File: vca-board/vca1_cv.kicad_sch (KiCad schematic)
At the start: 9 parts, among them U3 TL074

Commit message: VCA components linked
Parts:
- C10: footprint (none) -> Capacitor_SMD:C_0603_1608Metric_Pad1.08x0.95mm_HandSolder; LCSC (none) -> C76711
- C9: footprint (none) -> Capacitor_SMD:C_0603_1608Metric_Pad1.08x0.95mm_HandSolder; LCSC (none) -> C91367
- D3: footprint (none) -> Diode_SMD:D_SOD-523; LCSC (none) -> C131797
- D4: footprint (none) -> Diode_SMD:D_SOD-123; LCSC (none) -> C81598
- R21: footprint (none) -> Resistor_SMD:R_0201_0603Metric_Pad0.64x0.40mm_HandSolder; LCSC (none) -> C25811
- R24: footprint (none) -> Resistor_SMD:R_0201_0603Metric_Pad0.64x0.40mm_HandSolder; LCSC (none) -> C25803
- R25: LCSC (none) -> C22775
- R26: LCSC (none) -> C25804
- U3: footprint (none) -> Package_SO:SOIC-14_3.9x8.7mm_P1.27mm; LCSC (none) -> C6963
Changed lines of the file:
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@@
     (property "Reference" "R24" (id 0) (at 83.82 31.75 90))
     (property "Value" "100k" (id 1) (at 83.82 34.29 90))
-    (property "Footprint" "" (id 2) (at 83.82 39.878 90)
+    (property "Footprint" "Resistor_SMD:R_0201_0603Metric_Pad0.64x0.40mm_HandSolder" (id 2) (at 83.82 39.878 90)
       (effects (font (size 1.27 1.27)) hide)
     )
     (property "Datasheet" "~" (id 3) (at 83.82 38.1 0)
+      (effects (font (size 1.27 1.27)) hide)
+    )
+    (property "LCSC" "C25803" (id 4) (at 83.82 38.1 0)
       (effects (font (size 1.27 1.27)) hide)
     )
@@
       (effects (font (size 1.27 1.27)) hide)
     )
+    (property "LCSC" "C22775" (id 4) (at 99.06 53.34 0)
+      (effects (font (size 1.27 1.27)) hide)
+    )
     (pin "1")
     (pin "2")
@@
       (effects (font (size 1.27 1.27)) (justify left))
     )
-    (property "Footprint" "" (id 2) (at 106.68 66.04 0)
+    (property "Footprint" "Diode_SMD:D_SOD-523" (id 2) (at 106.68 66.04 0)
       (effects (font (size 1.27 1.27)) hide)
     )
     (property "Datasheet" "~" (id 3) (at 106.68 66.04 0)
+      (effects (font (size 1.27 1.27)) hide)
+    )
+    (property "LCSC" "C131797" (id 4) (at 106.68 66.04 0)
       (effects (font (size 1.27 1.27)) hide)
     )
@@
     (property "Reference" "C9" (id 0) (at 83.82 17.78 90))
     (property "Value" "10p" (id 1) (at 83.82 20.32 90))
-    (property "Footprint" "" (id 2) (at 87.63 24.4348 0)
+    (property "Footprint" "Capacitor_SMD:C_0603_1608Metric_Pad1.08x0.95mm_HandSolder" (id 2) (at 87.63 24.4348 0)
       (effects (font (size 1.27 1.27)) hide)
     )
@@
       (effects (font (size 1.27 1.27)) hide)
     )
+    (property "LCSC" "C91367" (id 4) (at 83.82 25.4 0)
+      (effects (font (size 1.27 1.27)) hide)
+    )
     (pin "1")
     (pin "2")
@@
     )
     (property "Datasheet" "~" (id 3) (at 140.97 60.96 0)
+      (effects (font (size 1.27 1.27)) hide)
+    )
+    (property "LCSC" "C25804" (id 4) (at 140.97 60.96 0)
       (effects (font (size 1.27 1.27)) hide)
     )
@@
     (property "Reference" "U3" (id 0) (at 119.38 40.64 0))
     (property "Value" "TL074" (id 1) (at 119.38 43.18 0))
-    (property "Footprint" "" (id 2) (at 118.11 53.34 0)
+    (property "Footprint" "Package_SO:SOIC-14_3.9x8.7mm_P1.27mm" (id 2) (at 118.11 53.34 0)
       (effects (font (size 1.27 1.27)) hide)
     )
     (property "Datasheet" "http://www.ti.com/lit/ds/symlink/tl071.pdf" (id 3) (at 120.65 55.88 0)
+      (effects (font (size 1.27 1.27)) hide)
+    )
+    (property "LCSC" "C6963" (id 4) (at 119.38 50.8 0)
       (effects (font (size 1.27 1.27)) hide)
     )
@@
       (effects (font (size 1.27 1.27)) (justify right))
     )
-    (property "Footprint" "" (id 2) (at 204.7748 46.99 0)
+    (property "Footprint" "Capacitor_SMD:C_0603_1608Metric_Pad1.08x0.95mm_HandSolder" (id 2) (at 204.7748 46.99 0)
       (effects (font (size 1.27 1.27)) hide)
     )
     (property "Datasheet" "~" (id 3) (at 205.74 50.8 0)
+      (effects (font (size 1.27 1.27)) hide)
+    )
+    (property "LCSC" "C76711" (id 4) (at 205.74 50.8 0)
       (effects (font (size 1.27 1.27)) hide)
     )
@@
     (property "Reference" "R21" (id 0) (at 68.58 44.45 90))
     (property "Value" "200k" (id 1) (at 68.58 46.99 90))
-    (property "Footprint" "" (id 2) (at 68.58 52.578 90)
+    (property "Footprint" "Resistor_SMD:R_0201_0603Metric_Pad0.64x0.40mm_HandSolder" (id 2) (at 68.58 52.578 90)
       (effects (font (size 1.27 1.27)) hide)
     )
@@
       (effects (font (size 1.27 1.27)) hide)
     )
+    (property "LCSC" "C25811" (id 4) (at 68.58 50.8 0)
+      (effects (font (size 1.27 1.27)) hide)
+    )
     (pin "1")
     (pin "2")
@@
       (effects (font (size 1.27 1.27)) (justify left))
     )
-    (property "Footprint" "" (id 2) (at 217.17 48.26 0)
+    (property "Footprint" "Package_SO:SOIC-14_3.9x8.7mm_P1.27mm" (id 2) (at 217.17 48.26 0)
       (effects (font (size 1.27 1.27)) hide)
     )
     (property "Datasheet" "http://www.ti.com/lit/ds/symlink/tl071.pdf" (id 3) (at 219.71 45.72 0)
+      (effects (font (size 1.27 1.27)) hide)
+    )
+    (property "LCSC" "C6963" (id 4) (at 218.44 50.8 0)
       (effects (font (size 1.27 1.27)) hide)
     )
@@
     (property "Reference" "D4" (id 0) (at 134.62 44.45 0))
     (property "Value" "D" (id 1) (at 134.62 46.99 0))
-    (property "Footprint" "" (id 2) (at 134.62 50.8 0)
+    (property "Footprint" "Diode_SMD:D_SOD-123" (id 2) (at 134.62 50.8 0)
       (effects (font (size 1.27 1.27)) hide)
     )
     (property "Datasheet" "~" (id 3) (at 134.62 50.8 0)
+      (effects (font (size 1.27 1.27)) hide)
+    )
+    (property "LCSC" "C81598" (id 4) (at 134.62 50.8 0)
       (effects (font (size 1.27 1.27)) hide)
     )
@@
     (property "Reference" "U3" (id 0) (at 83.82 43.18 0))
     (property "Value" "TL074" (id 1) (at 83.82 45.72 0))
-    (property "Footprint" "" (id 2) (at 82.55 55.88 0)
+    (property "Footprint" "Package_SO:SOIC-14_3.9x8.7mm_P1.27mm" (id 2) (at 82.55 55.88 0)
       (effects (font (size 1.27 1.27)) hide)
     )
@@
       (effects (font (size 1.27 1.27)) hide)
     )
+    (property "LCSC" "C6963" (id 4) (at 83.82 53.34 0)
+      (effects (font (size 1.27 1.27)) hide)
+    )

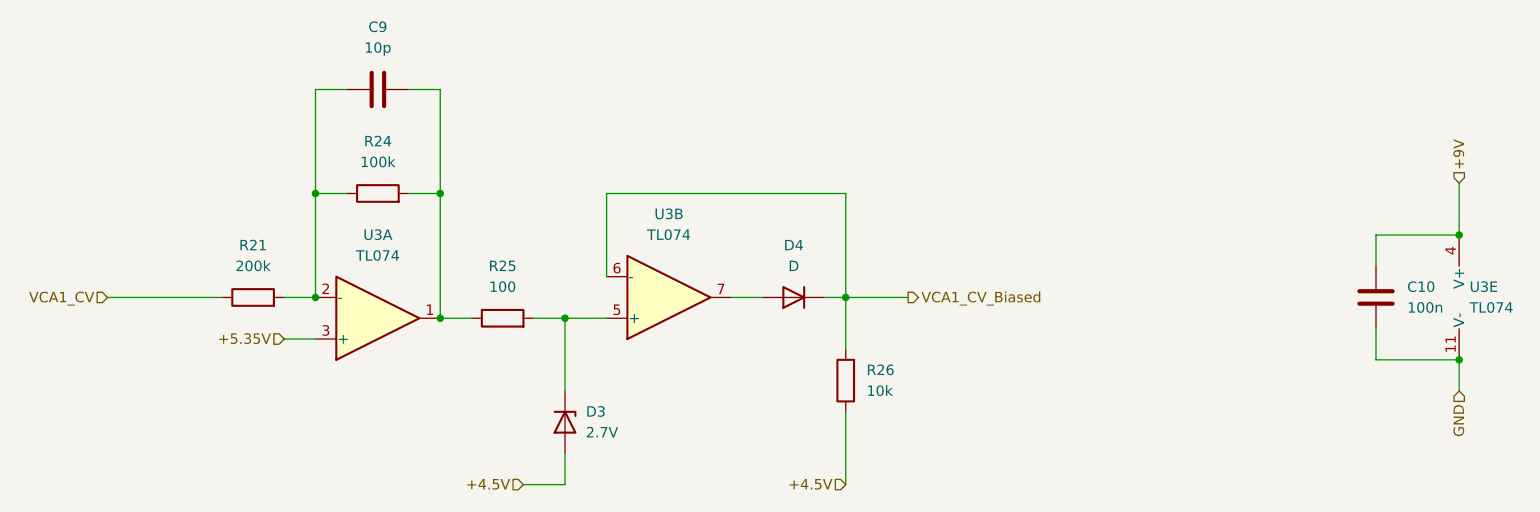
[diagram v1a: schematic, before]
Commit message: VCA board components placed
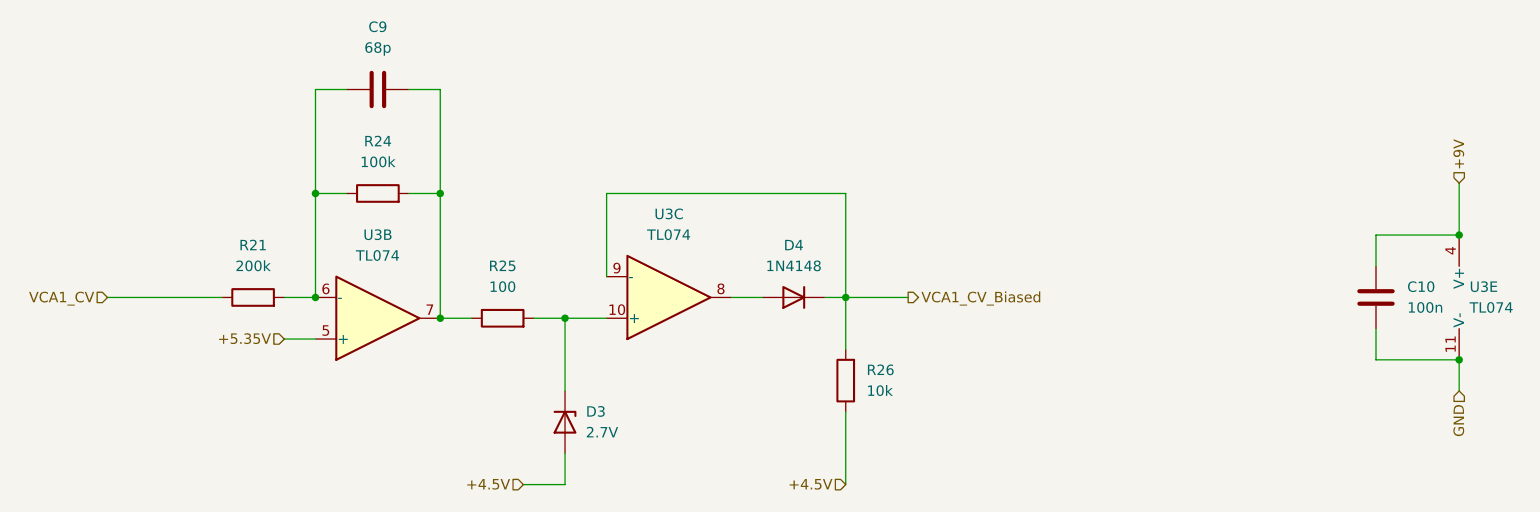
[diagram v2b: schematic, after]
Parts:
- C9: value 10p -> 68p; LCSC C91367 -> C1680
- D3: footprint Diode_SMD:D_SOD-523 -> Diode_SMD:D_SOD-123; LCSC C131797 -> C406712
- D4: value D -> 1N4148
- R21, R24: footprint Resistor_SMD:R_0201_0603Metric_Pad0.64x0.40mm_HandSolder -> Resistor_SMD:R_0603_1608Metric_Pad0.98x0.95mm_HandSolder
- R25, R26: footprint (none) -> Resistor_SMD:R_0603_1608Metric_Pad0.98x0.95mm_HandSolder
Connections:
- net +5.35V: now also U3.5 (+); no longer U3.3 (+)
- net VCA1_CV_Biased: now also U3.9 (-); no longer U3.6 (-)
- net at C9.1, R21.2, R24.1: now also U3.6 (-); no longer U3.2 (-)
- net at C9.2, R24.2, R25.1: now also U3.7; no longer U3.1
- net at D3.1 (K), R25.2: now also U3.10 (+); no longer U3.5 (+)
- net at D4.2 (A): now also U3.8; no longer U3.7
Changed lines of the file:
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@@
     (property "Reference" "R24" (id 0) (at 83.82 31.75 90))
     (property "Value" "100k" (id 1) (at 83.82 34.29 90))
-    (property "Footprint" "Resistor_SMD:R_0201_0603Metric_Pad0.64x0.40mm_HandSolder" (id 2) (at 83.82 39.878 90)
+    (property "Footprint" "Resistor_SMD:R_0603_1608Metric_Pad0.98x0.95mm_HandSolder" (id 2) (at 83.82 39.878 90)
       (effects (font (size 1.27 1.27)) hide)
     )
@@
     (property "Reference" "R25" (id 0) (at 99.06 46.99 90))
     (property "Value" "100" (id 1) (at 99.06 49.53 90))
-    (property "Footprint" "" (id 2) (at 99.06 55.118 90)
+    (property "Footprint" "Resistor_SMD:R_0603_1608Metric_Pad0.98x0.95mm_HandSolder" (id 2) (at 99.06 55.118 90)
       (effects (font (size 1.27 1.27)) hide)
     )
@@
       (effects (font (size 1.27 1.27)) (justify left))
     )
-    (property "Footprint" "Diode_SMD:D_SOD-523" (id 2) (at 106.68 66.04 0)
+    (property "Footprint" "Diode_SMD:D_SOD-123" (id 2) (at 106.68 66.04 0)
       (effects (font (size 1.27 1.27)) hide)
     )
@@
       (effects (font (size 1.27 1.27)) hide)
     )
-    (property "LCSC" "C131797" (id 4) (at 106.68 66.04 0)
+    (property "LCSC" "C406712" (id 4) (at 106.68 66.04 0)
       (effects (font (size 1.27 1.27)) hide)
     )
@@
     (in_bom yes) (on_board yes) (fields_autoplaced)
     (property "Reference" "C9" (id 0) (at 83.82 17.78 90))
-    (property "Value" "10p" (id 1) (at 83.82 20.32 90))
+    (property "Value" "68p" (id 1) (at 83.82 20.32 90))
     (property "Footprint" "Capacitor_SMD:C_0603_1608Metric_Pad1.08x0.95mm_HandSolder" (id 2) (at 87.63 24.4348 0)
       (effects (font (size 1.27 1.27)) hide)
@@
       (effects (font (size 1.27 1.27)) hide)
     )
-    (property "LCSC" "C91367" (id 4) (at 83.82 25.4 0)
+    (property "LCSC" "C1680" (id 4) (at 83.82 25.4 0)
       (effects (font (size 1.27 1.27)) hide)
     )
@@
       (effects (font (size 1.27 1.27)) (justify right))
     )
-    (property "Footprint" "" (id 2) (at 142.748 60.96 90)
+    (property "Footprint" "Resistor_SMD:R_0603_1608Metric_Pad0.98x0.95mm_HandSolder" (id 2) (at 142.748 60.96 90)
       (effects (font (size 1.27 1.27)) hide)
     )
@@
     (pin "2")
   )
-  (symbol (lib_id "Amplifier_Operational:TL074") (at 119.38 50.8 0) (mirror x) (unit 2)
+  (symbol (lib_id "Amplifier_Operational:TL074") (at 119.38 50.8 0) (mirror x) (unit 3)
     (in_bom yes) (on_board yes) (fields_autoplaced)
     (property "Reference" "U3" (id 0) (at 119.38 40.64 0))
@@
     (property "Reference" "R21" (id 0) (at 68.58 44.45 90))
     (property "Value" "200k" (id 1) (at 68.58 46.99 90))
-    (property "Footprint" "Resistor_SMD:R_0201_0603Metric_Pad0.64x0.40mm_HandSolder" (id 2) (at 68.58 52.578 90)
+    (property "Footprint" "Resistor_SMD:R_0603_1608Metric_Pad0.98x0.95mm_HandSolder" (id 2) (at 68.58 52.578 90)
       (effects (font (size 1.27 1.27)) hide)
     )
@@
     (in_bom yes) (on_board yes) (fields_autoplaced)
     (property "Reference" "D4" (id 0) (at 134.62 44.45 0))
-    (property "Value" "D" (id 1) (at 134.62 46.99 0))
+    (property "Value" "1N4148" (id 1) (at 134.62 46.99 0))
     (property "Footprint" "Diode_SMD:D_SOD-123" (id 2) (at 134.62 50.8 0)
       (effects (font (size 1.27 1.27)) hide)
@@
     (pin "2")
   )
-  (symbol (lib_id "Amplifier_Operational:TL074") (at 83.82 53.34 0) (mirror x) (unit 1)
+  (symbol (lib_id "Amplifier_Operational:TL074") (at 83.82 53.34 0) (mirror x) (unit 2)
     (in_bom yes) (on_board yes) (fields_autoplaced)
     (property "Reference" "U3" (id 0) (at 83.82 43.18 0))

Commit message: Remove D from linear VCA + update graphics
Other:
- company: (none) -> Pedal Markt / Andrey Salomatin
- title: (none) -> VCA Board
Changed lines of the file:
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@@
 (kicad_sch (version 20211123) (generator eeschema)
   (paper "A4")
+  (title_block
+    (title "VCA Board")
+    (date "2024-11-07")
+    (rev "v1rev2")
+    (company "Pedal Markt / Andrey Salomatin")
+  )
   (junction (at 76.2 38.1) (diameter 0) (color 0 0 0 0)
   )

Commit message: wip pre-redo orientation
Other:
- company: Pedal Markt / Andrey Salomatin -> Andrey Salomatin / Pedal Markt
- title: VCA Board -> Mag
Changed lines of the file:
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@@
   (paper "A4")
   (title_block
-    (title "VCA Board")
+    (title "Mag")
     (date "2024-11-07")
     (rev "v1rev2")
-    (company "Pedal Markt / Andrey Salomatin")
+    (company "Andrey Salomatin / Pedal Markt")
   )
   (junction (at 76.2 38.1) (diameter 0) (color 0 0 0 0)
